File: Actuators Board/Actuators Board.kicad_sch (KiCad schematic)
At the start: 71 parts, among them J1 Conn_01x05_Male, J10 Conn_01x02_Male, J2 Solenoid(Sol), J4 Conn_01x03_Male, J5 Conn_01x06_Male, J9 Conn_01x02_Male, Q1 MMDT2222A, Q2 SI2366DS, U1 ESP32-PICO-D4, U2 TPS54233D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

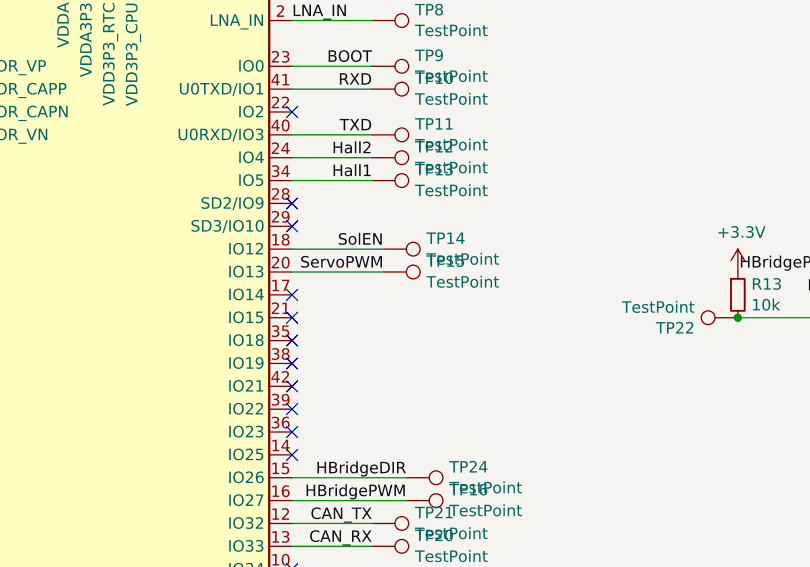
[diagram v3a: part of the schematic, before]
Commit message: autoboot circuit layout
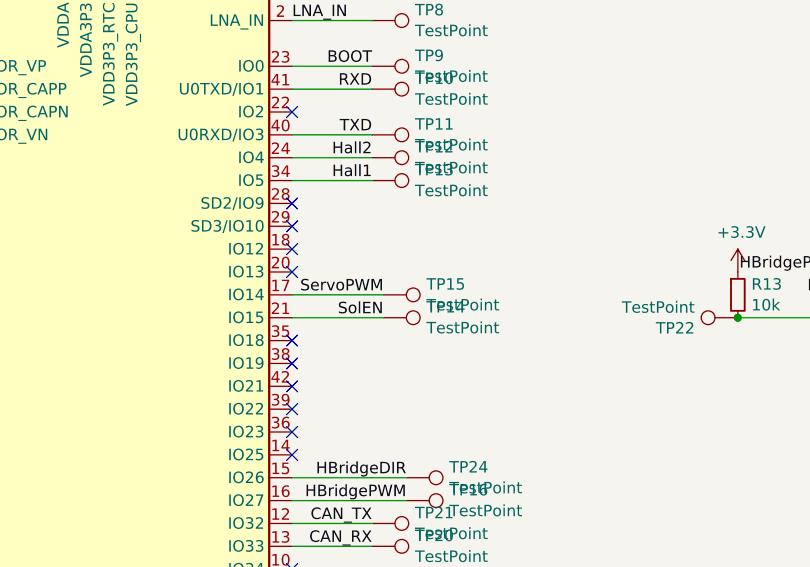
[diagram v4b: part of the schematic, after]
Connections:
- net ServoPWM: now also U1.17 (IO14); no longer U1.20 (IO13)
- net SolEN: now also U1.21 (IO15); no longer U1.18 (IO12)
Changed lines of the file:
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@@
   (no_connect (at 93.98 96.52))
   (no_connect (at 134.62 129.54))
+  (no_connect (at 134.62 88.9))
   (no_connect (at 93.98 99.06))
   (no_connect (at 134.62 121.92))
@@
   (no_connect (at 93.98 106.68))
   (no_connect (at 134.62 124.46))
+  (no_connect (at 134.62 86.36))
   (no_connect (at 134.62 81.28))
   (no_connect (at 93.98 109.22))
@@
   (no_connect (at 93.98 73.66))
   (no_connect (at 134.62 104.14))
-  (no_connect (at 134.62 91.44))
   (no_connect (at 134.62 101.6))
-  (no_connect (at 134.62 93.98))
   (no_connect (at 134.62 106.68))
   (wire (pts (xy 30.48 191.77) (xy 30.48 190.5))
@@
     (stroke (width 0) (type default) (color 0 0 0 0))
   )
-  (wire (pts (xy 134.62 88.9) (xy 144.78 88.9))
-    (stroke (width 0) (type default) (color 0 0 0 0))
-  )
   (wire (pts (xy 269.24 39.37) (xy 269.24 41.91))
     (stroke (width 0) (type default) (color 0 0 0 0))
@@
     (stroke (width 0) (type default) (color 0 0 0 0))
   )
-  (wire (pts (xy 134.62 86.36) (xy 144.78 86.36))
-    (stroke (width 0) (type default) (color 0 0 0 0))
-  )
   (wire (pts (xy 97.79 52.07) (xy 100.33 52.07))
     (stroke (width 0) (type default) (color 0 0 0 0))
@@
     (stroke (width 0) (type default) (color 0 0 0 0))
   )
+  (wire (pts (xy 134.62 93.98) (xy 144.78 93.98))
+    (stroke (width 0) (type default) (color 0 0 0 0))
+  )
+  (wire (pts (xy 134.62 91.44) (xy 144.78 91.44))
+    (stroke (width 0) (type default) (color 0 0 0 0))
+  )
   (wire (pts (xy 134.62 119.38) (xy 143.51 119.38))
     (stroke (width 0) (type default) (color 0 0 0 0))
@@
     (effects (font (size 1.27 1.27)) (justify left bottom))
   )
+  (label "SolEN" (at 139.7 93.98 0)
+    (effects (font (size 1.27 1.27)) (justify left bottom))
+  )
   (label "DTR" (at 34.29 74.93 180)
     (effects (font (size 1.27 1.27)) (justify right bottom))
@@
     (effects (font (size 1.27 1.27)) (justify right bottom))
   )
+  (label "ServoPWM" (at 144.78 91.44 180)
+    (effects (font (size 1.27 1.27)) (justify right bottom))
+  )
   (label "Hall1" (at 143.51 78.74 180)
     (effects (font (size 1.27 1.27)) (justify right bottom))
@@
     (effects (font (size 1.27 1.27)) (justify left bottom))
   )
-  (label "ServoPWM" (at 144.78 88.9 180)
-    (effects (font (size 1.27 1.27)) (justify right bottom))
-  )
   (label "BOOT" (at 73.66 165.1 180)
     (effects (font (size 1.27 1.27)) (justify right bottom))
@@
     (effects (font (size 1.27 1.27)) (justify right bottom))
   )
-  (label "SolEN" (at 139.7 86.36 0)
-    (effects (font (size 1.27 1.27)) (justify left bottom))
-  )
   (label "RXD" (at 17.78 21.59 0)
     (effects (font (size 1.27 1.27)) (justify left bottom))
@@
     (pin "5")
   )
-  (symbol (lib_id "Connector:TestPoint") (at 144.78 88.9 270) (unit 1)
-    (in_bom yes) (on_board yes)
-    (property "Reference" "TP15" (id 0) (at 149.5552 87.7316 90)
-      (effects (font (size 1.27 1.27)) (justify left))
-    )
-    (property "Value" "TestPoint" (id 1) (at 149.5552 90.043 90)
-      (effects (font (size 1.27 1.27)) (justify left))
-    )
-    (property "Footprint" "TestPoint:TestPoint_THTPad_1.0x1.0mm_Drill0.5mm" (id 2) (at 144.78 93.98 0)
-      (effects (font (size 1.27 1.27)) hide)
-    )
-    (property "Datasheet" "~" (id 3) (at 144.78 93.98 0)
-      (effects (font (size 1.27 1.27)) hide)
-    )
-    (pin "1")
-  )
   (symbol (lib_id "Connector:TestPoint") (at 143.51 73.66 270) (unit 1)
     (in_bom yes) (on_board yes)
@@
     (pin "1")
   )
-  (symbol (lib_id "Connector:TestPoint") (at 144.78 86.36 270) (unit 1)
+  (symbol (lib_id "Device:LED_Small") (at 48.26 30.48 180) (unit 1)
     (in_bom yes) (on_board yes)
-    (property "Reference" "TP14" (id 0) (at 149.5552 85.1916 90)
+    (property "Reference" "D1" (id 0) (at 48.26 25.273 0))
+    (property "Value" "Solenoid LED" (id 1) (at 48.26 27.5844 0))
+    (property "Footprint" "LED_SMD:LED_0603_1608Metric" (id 2) (at 48.26 30.48 90)
+      (effects (font (size 1.27 1.27)) hide)
+    )
+    (property "Datasheet" "~" (id 3) (at 48.26 30.48 90)
+      (effects (font (size 1.27 1.27)) hide)
+    )
+    (pin "1")
+    (pin "2")
+  )
+  (symbol (lib_id "Connector:TestPoint") (at 144.78 93.98 270) (unit 1)
+    (in_bom yes) (on_board yes)
+    (property "Reference" "TP14" (id 0) (at 149.5552 92.8116 90)
       (effects (font (size 1.27 1.27)) (justify left))
     )
-    (property "Value" "TestPoint" (id 1) (at 149.5552 87.503 90)
+    (property "Value" "TestPoint" (id 1) (at 149.5552 95.123 90)
       (effects (font (size 1.27 1.27)) (justify left))
     )
-    (property "Footprint" "TestPoint:TestPoint_THTPad_1.0x1.0mm_Drill0.5mm" (id 2) (at 144.78 91.44 0)
+    (property "Footprint" "TestPoint:TestPoint_THTPad_1.0x1.0mm_Drill0.5mm" (id 2) (at 144.78 99.06 0)
       (effects (font (size 1.27 1.27)) hide)
     )
-    (property "Datasheet" "~" (id 3) (at 144.78 91.44 0)
+    (property "Datasheet" "~" (id 3) (at 144.78 99.06 0)
       (effects (font (size 1.27 1.27)) hide)
     )
     (pin "1")
   )
-  (symbol (lib_id "Device:LED_Small") (at 48.26 30.48 180) (unit 1)
+  (symbol (lib_id "Connector:TestPoint") (at 144.78 91.44 270) (unit 1)
     (in_bom yes) (on_board yes)
-    (property "Reference" "D1" (id 0) (at 48.26 25.273 0))
-    (property "Value" "Solenoid LED" (id 1) (at 48.26 27.5844 0))
-    (property "Footprint" "LED_SMD:LED_0603_1608Metric" (id 2) (at 48.26 30.48 90)
+    (property "Reference" "TP15" (id 0) (at 149.5552 90.2716 90)
+      (effects (font (size 1.27 1.27)) (justify left))
+    )
+    (property "Value" "TestPoint" (id 1) (at 149.5552 92.583 90)
+      (effects (font (size 1.27 1.27)) (justify left))
+    )
+    (property "Footprint" "TestPoint:TestPoint_THTPad_1.0x1.0mm_Drill0.5mm" (id 2) (at 144.78 96.52 0)
       (effects (font (size 1.27 1.27)) hide)
     )
-    (property "Datasheet" "~" (id 3) (at 48.26 30.48 90)
+    (property "Datasheet" "~" (id 3) (at 144.78 96.52 0)
       (effects (font (size 1.27 1.27)) hide)
     )
     (pin "1")
-    (pin "2")
   )
   (sheet (at 30.48 81.28) (size 25.4 12.7) (fields_autoplaced)
@@
     )
     (path "/00000000-0000-0000-0000-000061a24258/00000000-0000-0000-0000-000061a4fe2f"
-      (reference "L1") (unit 1) (value "LQG15WZ1N8B02D") (footprint "Inductor_SMD:L_0402_1005Metric_Pad0.77x0.64mm_HandSolder")
+      (reference "L1") (unit 1) (value "LQG15WZ1N8B02D") (footprint "Inductor_SMD:L_0603_1608Metric_Pad1.05x0.95mm_HandSolder")
     )
     (path "/00000000-0000-0000-0000-00006199cc35"
@@
       (reference "TP13") (unit 1) (value "TestPoint") (footprint "TestPoint:TestPoint_THTPad_1.0x1.0mm_Drill0.5mm")
     )
-    (path "/00000000-0000-0000-0000-000061da1b39"
+    (path "/0bdf33f6-bc5a-4a83-84e7-d8a9aa36e060"
       (reference "TP14") (unit 1) (value "TestPoint") (footprint "TestPoint:TestPoint_THTPad_1.0x1.0mm_Drill0.5mm")
     )
-    (path "/00000000-0000-0000-0000-000061b0e262"
+    (path "/d69380f9-5487-4782-9ce9-0690df62e543"
       (reference "TP15") (unit 1) (value "TestPoint") (footprint "TestPoint:TestPoint_THTPad_1.0x1.0mm_Drill0.5mm")
     )

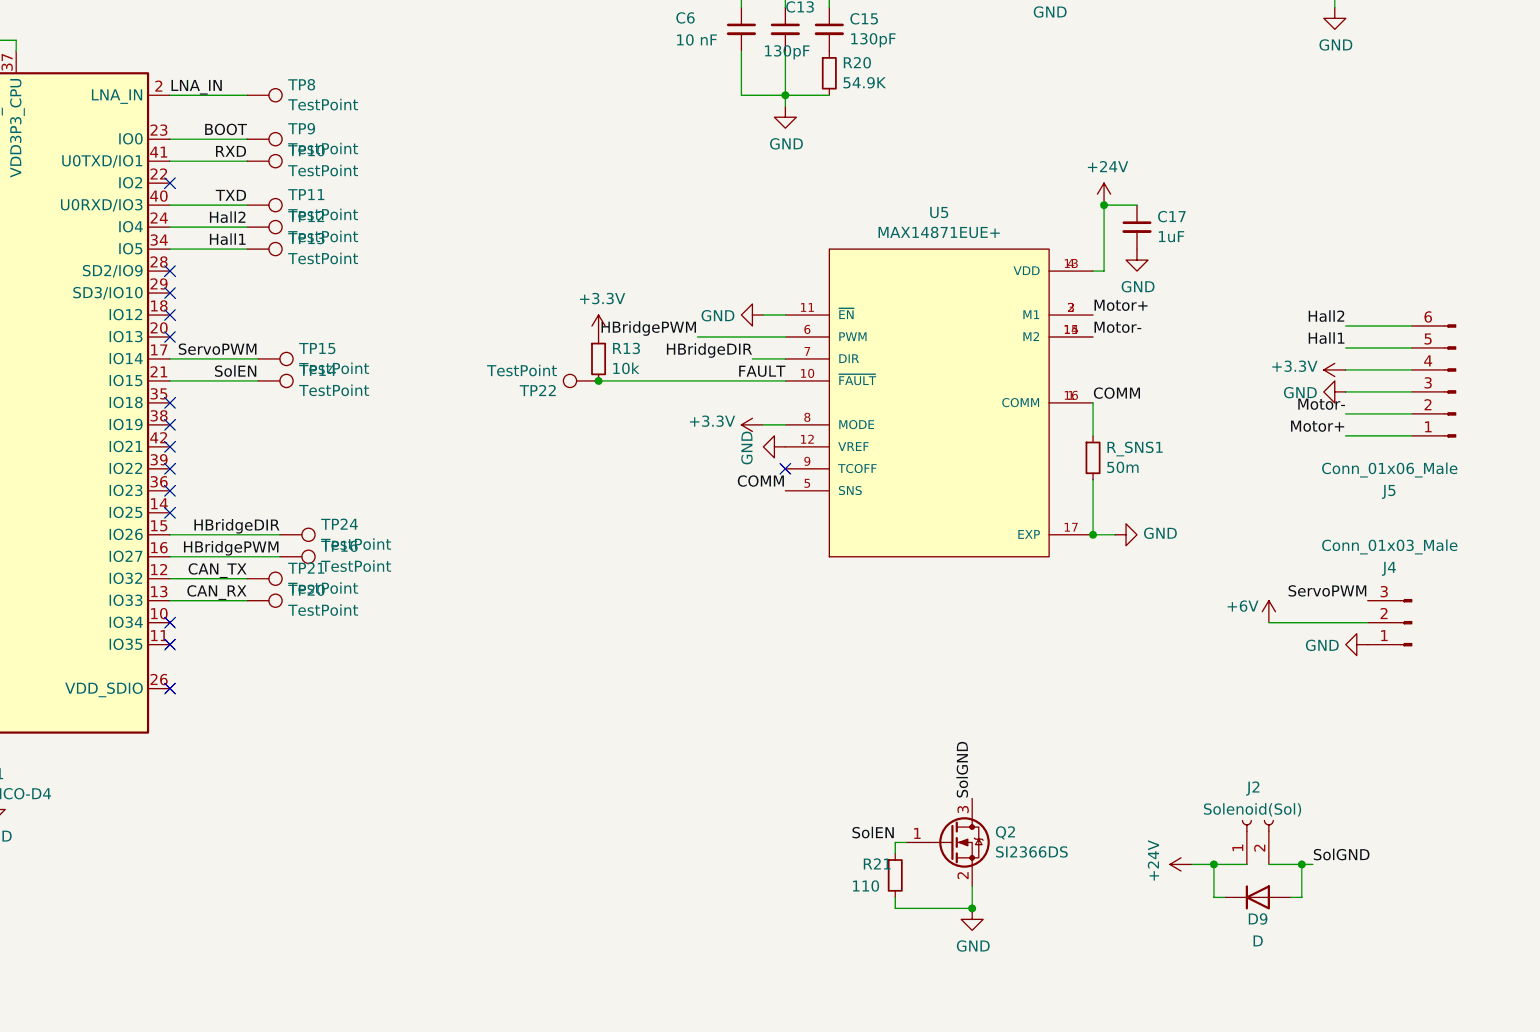
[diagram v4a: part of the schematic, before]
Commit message: Swapped h-bridge with new one, combined the PCBs and some layout
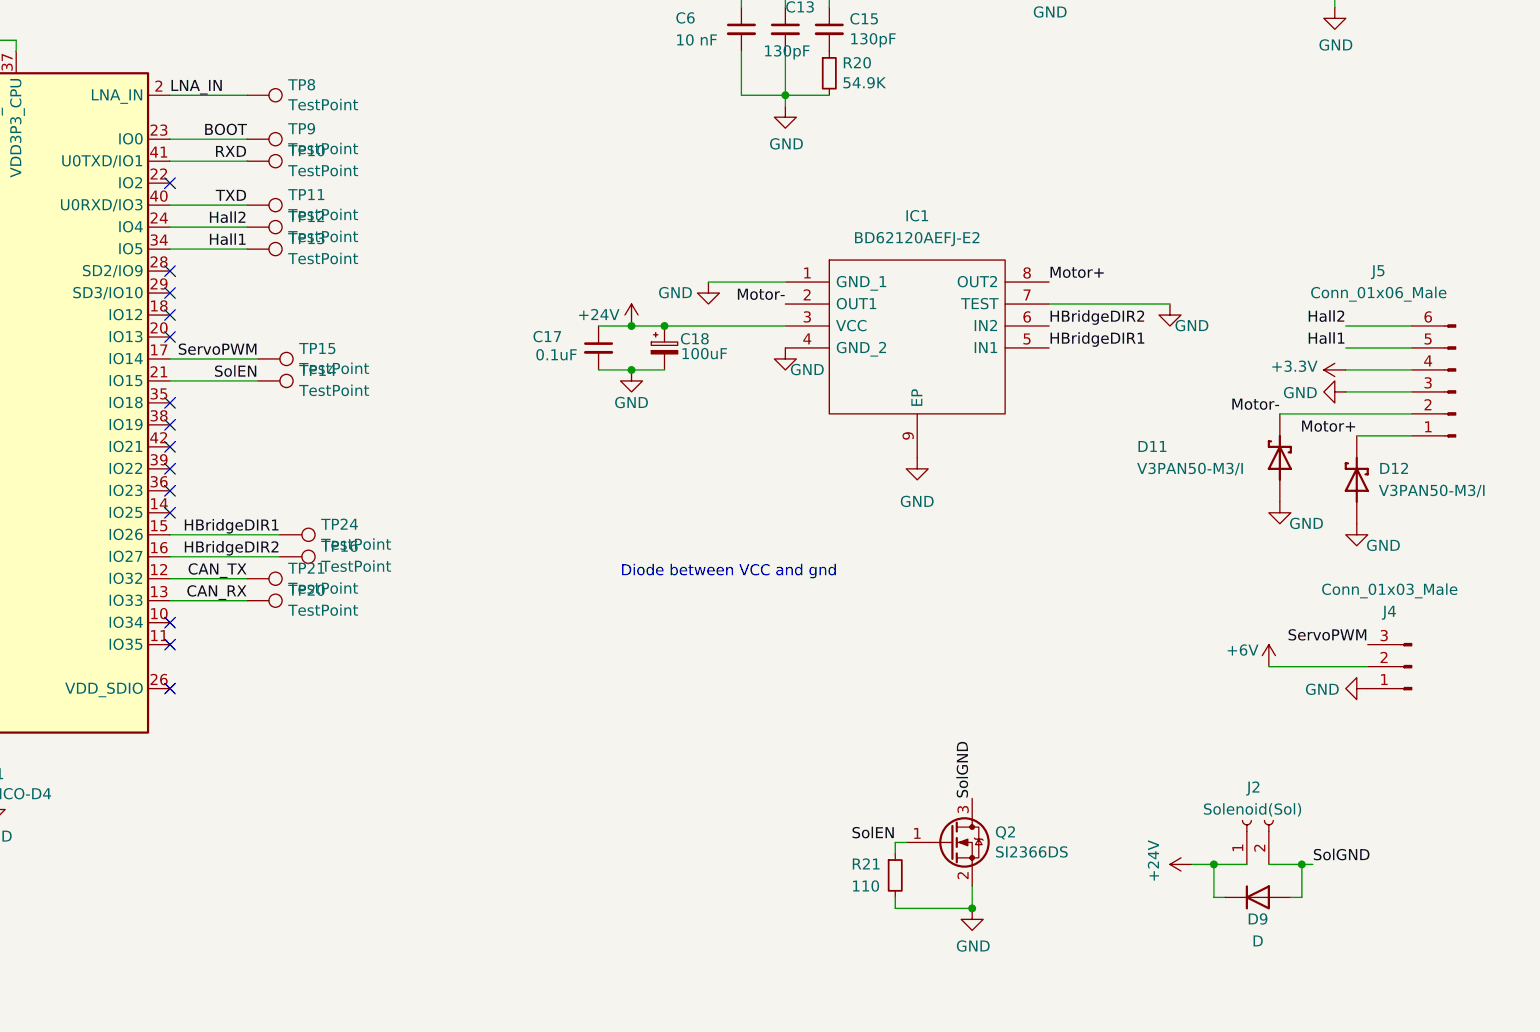
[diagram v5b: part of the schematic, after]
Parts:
- removed R13: 10k, Resistor_SMD:R_0603_1608Metric, symbol Device:R_Small
- removed R_SNS1: 50m, Resistor_SMD:R_0603_1608Metric, symbol Device:R_Small
- removed TP22: TestPoint, TestPoint:TestPoint_THTPad_1.0x1.0mm_Drill0.5mm, symbol Connector:TestPoint
- removed U5: MAX14871EUE+, iclr:SOP65P637X110-16N, symbol iclr:MAX14871EUE+
- added C18: 100uF, Capacitor_SMD:CP_Elec_5x5.9, symbol Device:C_Polarized_Small
- added D11, D12: V3PAN50-M3/I, iclr:DIO_V3PAN50-M3_I, symbol iclr:V3PAN50-M3{brace}slash}I
- added IC1: BD62120AEFJ-E2, iclr:SOIC127P600X100-9N, symbol iclr:BD62120AEFJ-E2
- C17: value 1uF -> 0.1uF
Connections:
- net +24V: now also C18.1, IC1.3 (VCC)
- net GND: now also C18.2, D11.A, D12.A, IC1.1 (GND_1), IC1.4 (GND_2), IC1.7 (TEST), IC1.9 (EP)
- net Motor+: now also D12.C, IC1.8 (OUT2)
- net Motor-: now also D11.C, IC1.2 (OUT1)
- net HBridgeDIR renamed HBridgeDIR1
- net HBridgeDIR1: now also IC1.5 (IN1)
- net HBridgePWM renamed HBridgeDIR2
- net HBridgeDIR2: now also IC1.6 (IN2)
- no-connect marks 26 -> 25
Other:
- note added: "Diode between VCC and gnd"
- moved on the sheet: J4

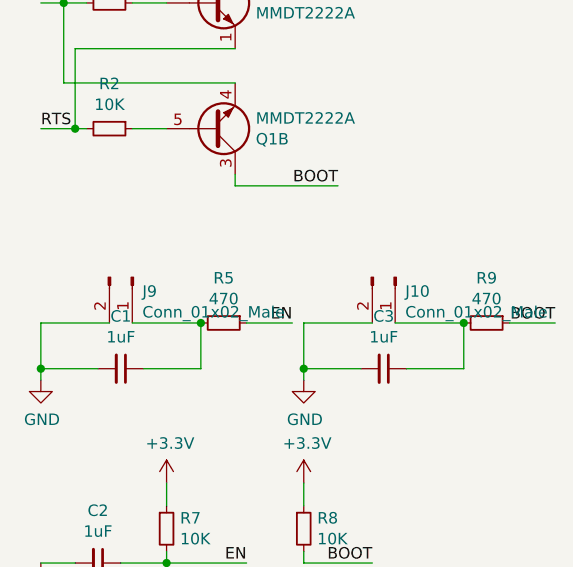
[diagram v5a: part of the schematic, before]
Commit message: Fully connected autoboot circuit and jumpers.
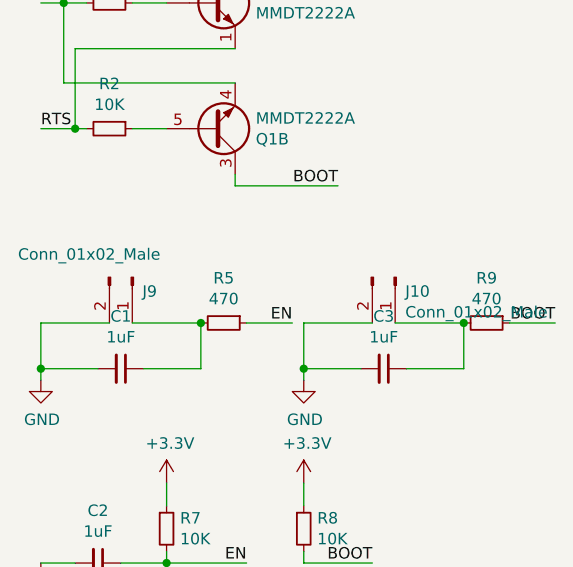
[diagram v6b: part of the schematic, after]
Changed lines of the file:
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@@
       (effects (font (size 1.27 1.27)) (justify left))
     )
-    (property "Value" "Conn_01x02_Male" (id 1) (at 27.7876 163.9062 90)
+    (property "Value" "Conn_01x02_Male" (id 1) (at 13.97 157.48 90)
       (effects (font (size 1.27 1.27)) (justify left))
     )

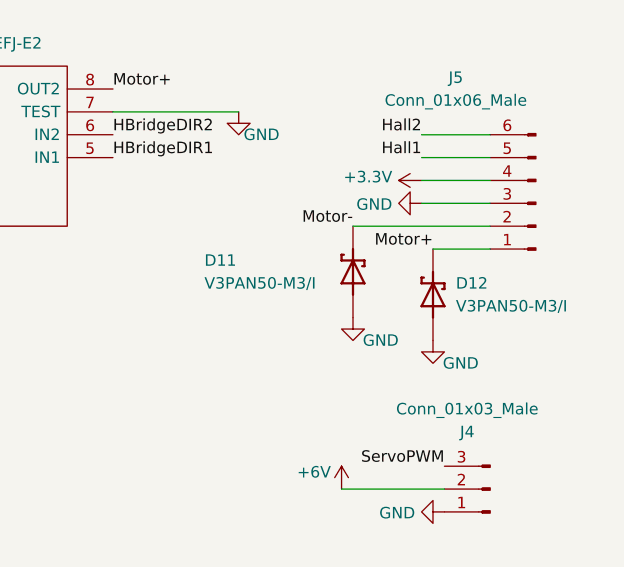
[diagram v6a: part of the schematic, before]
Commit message: Changed schottky diode name
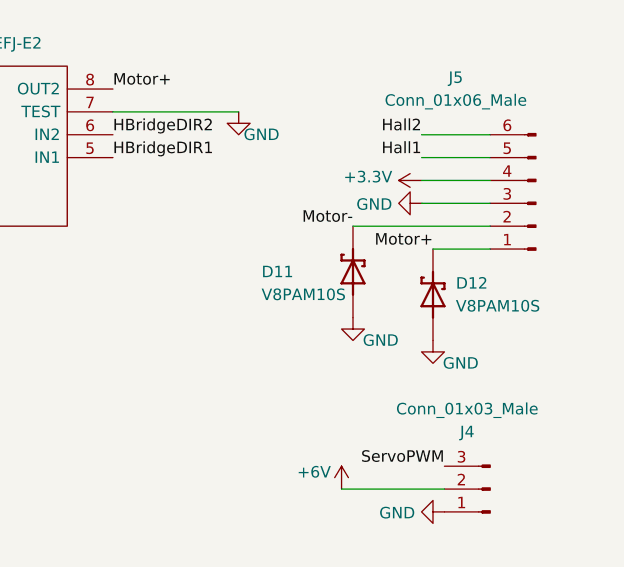
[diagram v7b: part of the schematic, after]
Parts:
- D11, D12: value V3PAN50-M3/I -> V8PAM10S
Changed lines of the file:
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@@
       (effects (font (size 1.27 1.27)) (justify right))
     )
-    (property "Value" "V3PAN50-M3{slash}I" (id 1) (at 274.32 106.6799 90)
+    (property "Value" "V8PAM10S" (id 1) (at 274.32 106.6799 90)
       (effects (font (size 1.27 1.27)) (justify right))
     )
@@
   (symbol (lib_id "iclr:V3PAN50-M3{brace}slash}I") (at 262.89 102.87 90) (unit 1)
     (in_bom yes) (on_board yes)
-    (property "Reference" "D11" (id 0) (at 246.38 101.6 90)
-      (effects (font (size 1.27 1.27)) (justify right))
-    )
-    (property "Value" "V3PAN50-M3{slash}I" (id 1) (at 246.38 104.14 90)
+    (property "Reference" "D11" (id 0) (at 252.73 102.87 90)
+      (effects (font (size 1.27 1.27)) (justify right))
+    )
+    (property "Value" "V8PAM10S" (id 1) (at 252.73 105.41 90)
       (effects (font (size 1.27 1.27)) (justify right))
     )
@@
     )
     (path "/fdfb32b0-7ffe-426f-9d80-1deb6639eb2a"
-      (reference "D11") (unit 1) (value "V3PAN50-M3{slash}I") (footprint "iclr:DIO_V3PAN50-M3_I")
+      (reference "D11") (unit 1) (value "V8PAM10S") (footprint "iclr:DIO_V3PAN50-M3_I")
     )
     (path "/5f1a3709-f26d-431b-98e3-0a96203045fb"
-      (reference "D12") (unit 1) (value "V3PAN50-M3{slash}I") (footprint "iclr:DIO_V3PAN50-M3_I")
+      (reference "D12") (unit 1) (value "V8PAM10S") (footprint "iclr:DIO_V3PAN50-M3_I")
     )
     (path "/a9ca37b3-d0be-4022-acd0-baf378937a34"
